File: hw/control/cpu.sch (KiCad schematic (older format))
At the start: 2 parts

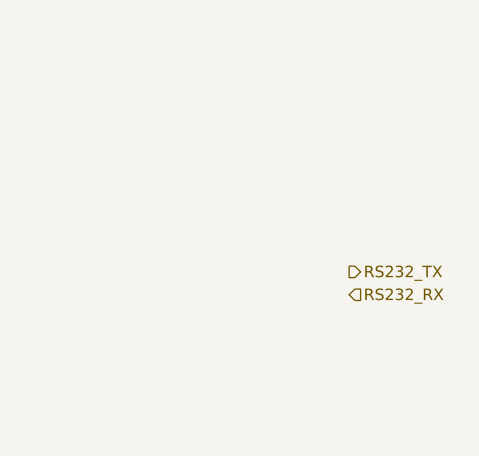
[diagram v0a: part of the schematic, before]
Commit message: [hw] Add LED bus driver
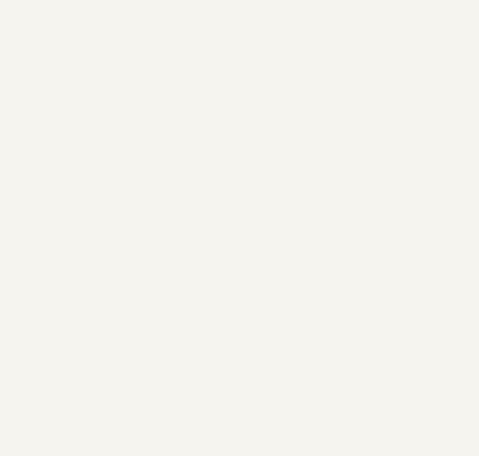
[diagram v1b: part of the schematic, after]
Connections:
- net labels removed: RS232_RX, RS232_TX
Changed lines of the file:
@@
 Wire Wire Line
 	5000 3450 6850 3450
-Text HLabel 9450 5000 2    50   Output ~ 0
-RS232_TX
-Text HLabel 9450 5100 2    50   Input ~ 0
-RS232_RX
 $EndSCHEMATC

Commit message: [hw] Add secondary SD card connection
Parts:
- added C?: 100n, symbol Device:C
- added J?: Conn_01x03_Male, symbol Connector:Conn_01x03_Male
- added J?: Micro_SD_Card, symbol Connector:Micro_SD_Card
- added R? (x6): 33R, symbol Device:R
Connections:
- wire segments 34 -> 80
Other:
- moved on the sheet: J?

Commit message: [hw] Add annotations, minor fixes
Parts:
- removed J?: Raspberry_Pi_2_3, symbol Connector:Raspberry_Pi_2_3
- added C301, C302, C303, C304: 100n, symbol Device:C
- added J303: Raspberry_Pi_0_2_3, symbol my:Raspberry_Pi_0_2_3
- gave numbers to parts that had none: 10
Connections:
- wire segments 80 -> 108
- no-connect marks 0 -> 3

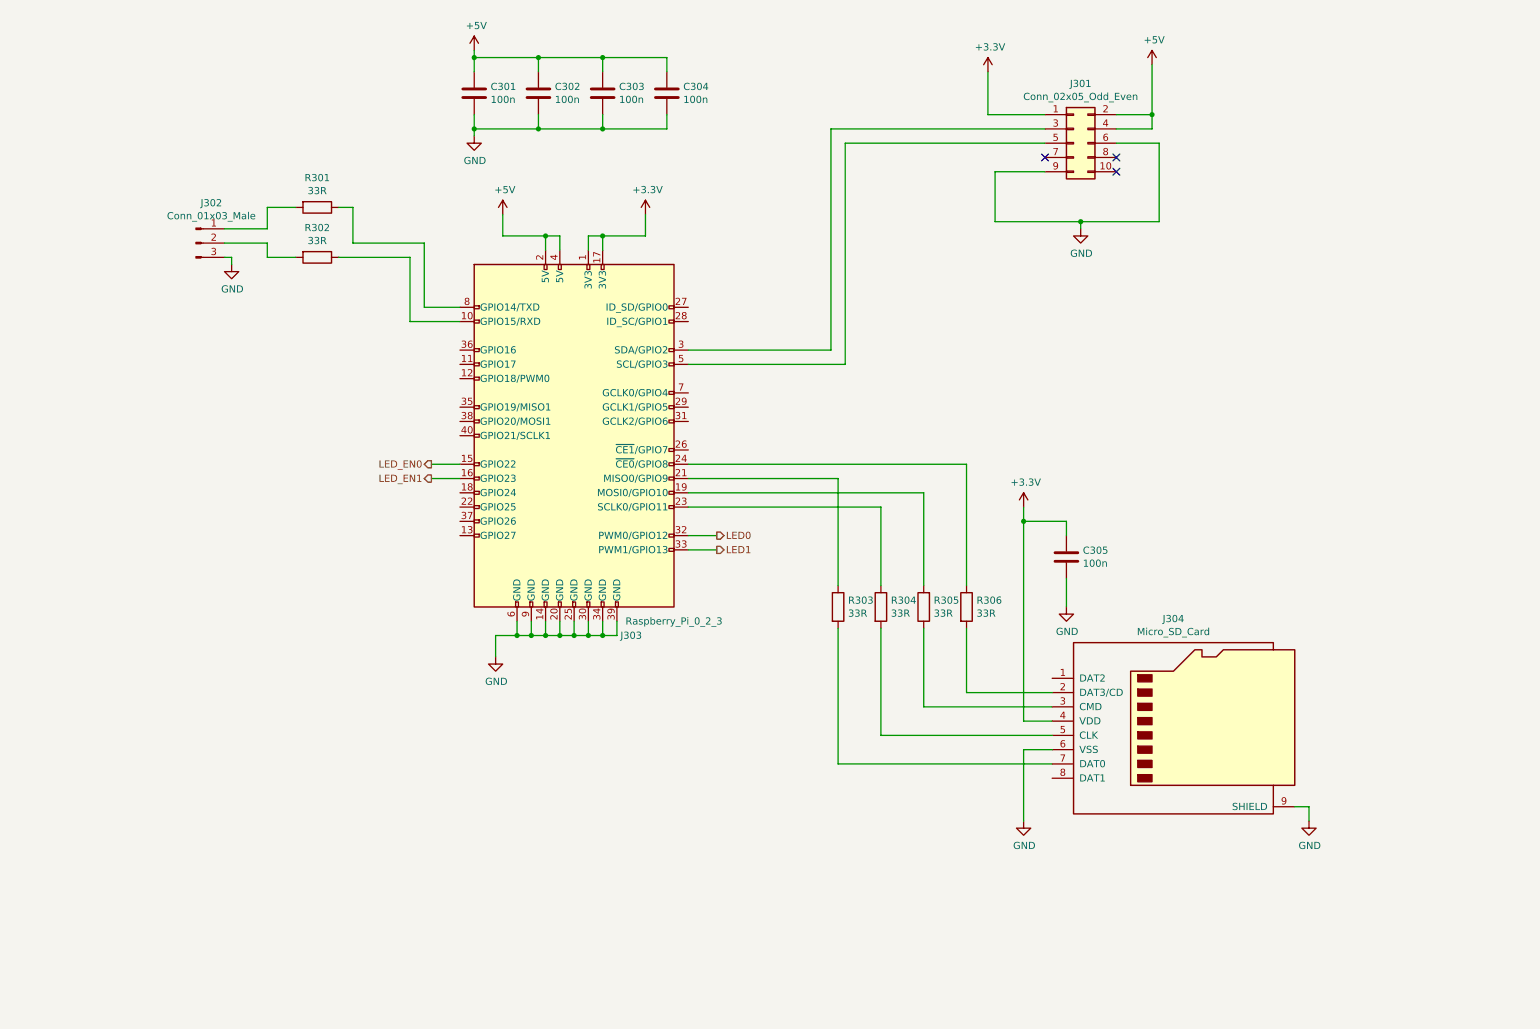
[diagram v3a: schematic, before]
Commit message: [hw] Add LED driver output sheets
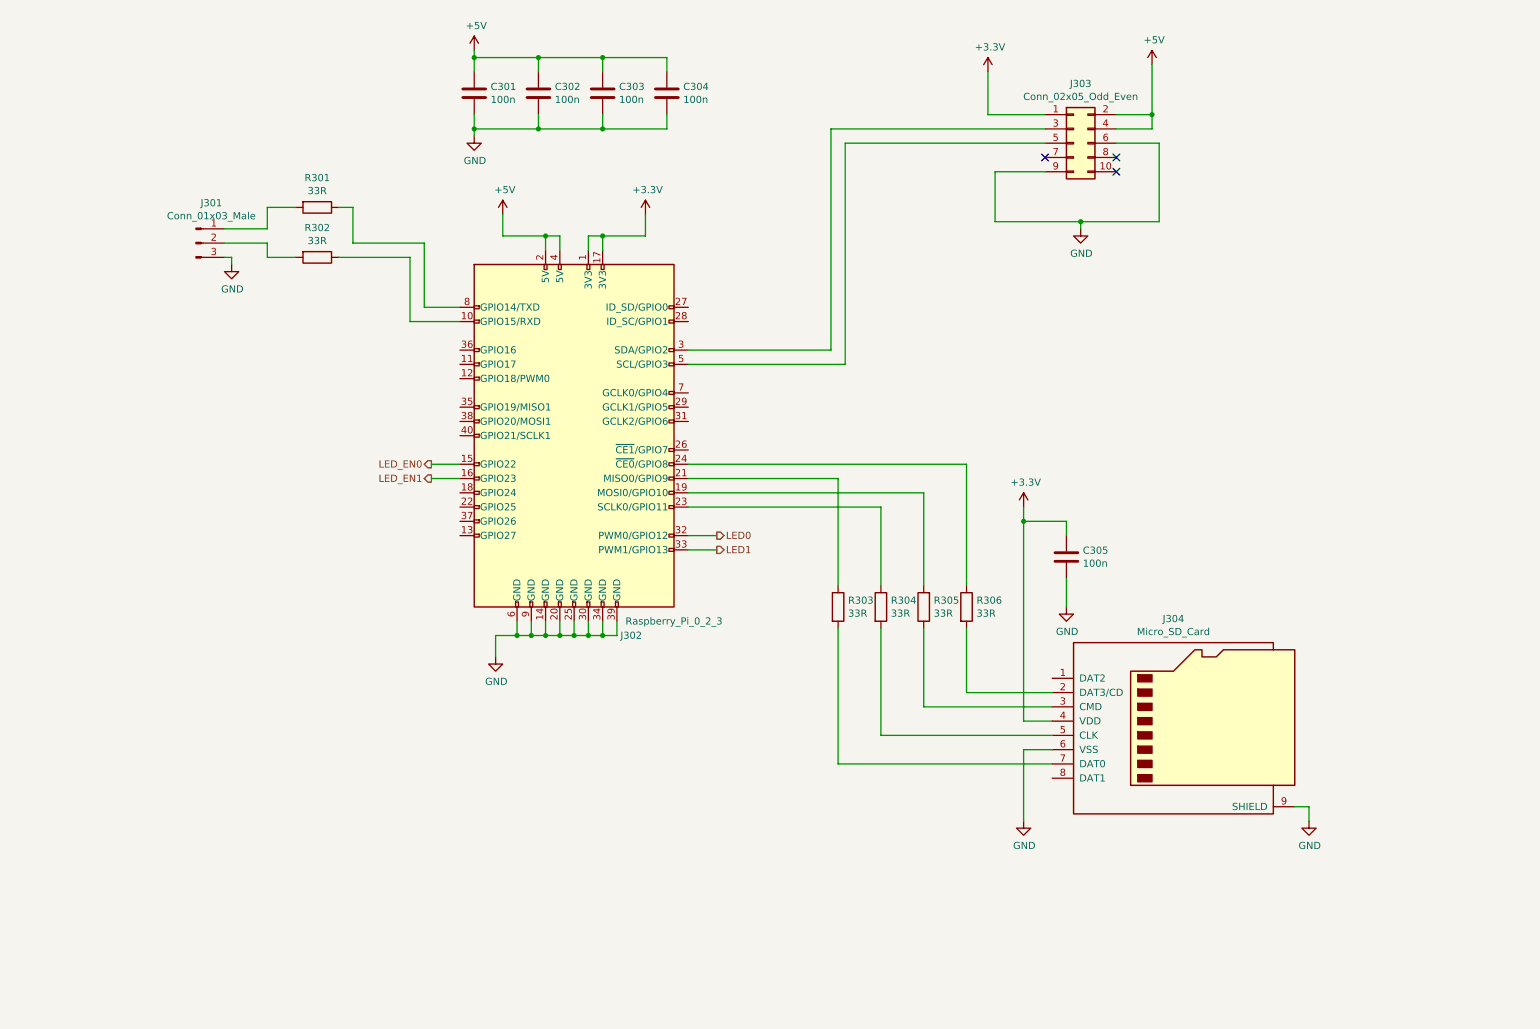
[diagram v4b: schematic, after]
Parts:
- renumbered J302 to J301, J303 to J302, J301 to J303
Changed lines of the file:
@@
 $Descr A4 11693 8268
 encoding utf-8
-Sheet 3 7
+Sheet 3 9
 Title "WS2812 Controller"
-Date "2021-09-16"
+Date "2021-09-21"
 Rev "1"
 Comp "Stefan Misik"
@@
 P 3950 5100
 AR Path="/614A2C71" Ref="#PWR?"  Part="1"
-AR Path="/6148E1AC/614A2C71" Ref="#PWR0311"  Part="1"
-F 0 "#PWR0311" H 3950 4850 50  0001 C CNN
+AR Path="/6148E1AC/614A2C71" Ref="#PWR0304"  Part="1"
+F 0 "#PWR0304" H 3950 4850 50  0001 C CNN
 F 1 "GND" H 3955 4927 50  0000 C CNN
 F 2 "" H 3950 5100 50  0001 C CNN
@@
 P 8000 1500
 AR Path="/614A2C9B" Ref="J?"  Part="1"
-AR Path="/6148E1AC/614A2C9B" Ref="J301"  Part="1"
-F 0 "J301" H 8050 1917 50  0000 C CNN
+AR Path="/6148E1AC/614A2C9B" Ref="J303"  Part="1"
+F 0 "J303" H 8050 1917 50  0000 C CNN
 F 1 "Conn_02x05_Odd_Even" H 8050 1826 50  0000 C CNN
 F 2 "" H 8000 1500 50  0001 C CNN
@@
 P 8550 950
 AR Path="/614A2CA1" Ref="#PWR?"  Part="1"
-AR Path="/6148E1AC/614A2CA1" Ref="#PWR0302"  Part="1"
-F 0 "#PWR0302" H 8550 800 50  0001 C CNN
+AR Path="/6148E1AC/614A2CA1" Ref="#PWR0312"  Part="1"
+F 0 "#PWR0312" H 8550 800 50  0001 C CNN
 F 1 "+5V" H 8565 1123 50  0000 C CNN
 F 2 "" H 8550 950 50  0001 C CNN
@@
 P 7400 1000
 AR Path="/614A2CA7" Ref="#PWR?"  Part="1"
-AR Path="/6148E1AC/614A2CA7" Ref="#PWR0303"  Part="1"
-F 0 "#PWR0303" H 7400 850 50  0001 C CNN
+AR Path="/6148E1AC/614A2CA7" Ref="#PWR0307"  Part="1"
+F 0 "#PWR0307" H 7400 850 50  0001 C CNN
 F 1 "+3.3V" H 7415 1173 50  0000 C CNN
 F 2 "" H 7400 1000 50  0001 C CNN
@@
 P 8050 2100
 AR Path="/614A2CB4" Ref="#PWR?"  Part="1"
-AR Path="/6148E1AC/614A2CB4" Ref="#PWR0307"  Part="1"
-F 0 "#PWR0307" H 8050 1850 50  0001 C CNN
+AR Path="/6148E1AC/614A2CB4" Ref="#PWR0311"  Part="1"
+F 0 "#PWR0311" H 8050 1850 50  0001 C CNN
 F 1 "GND" H 8055 1927 50  0000 C CNN
 F 2 "" H 8050 2100 50  0001 C CNN
@@
 LED_EN1
 $Comp
-L Connector:Conn_01x03_Male J302
+L Connector:Conn_01x03_Male J301
 U 1 1 614671E5
 P 1850 2200
-F 0 "J302" H 1958 2481 50  0000 C CNN
+F 0 "J301" H 1958 2481 50  0000 C CNN
 F 1 "Conn_01x03_Male" H 1958 2390 50  0000 C CNN
 F 2 "" H 1850 2200 50  0001 C CNN
@@
 $EndComp
 $Comp
-L power:GND #PWR0308
+L power:GND #PWR0301
 U 1 1 6146B045
 P 2100 2350
-F 0 "#PWR0308" H 2100 2100 50  0001 C CNN
+F 0 "#PWR0301" H 2100 2100 50  0001 C CNN
 F 1 "GND" H 2105 2177 50  0000 C CNN
 F 2 "" H 2100 2350 50  0001 C CNN
@@
 	6950 3950 6950 4600
 $Comp
-L power:+3.3V #PWR0309
+L power:+3.3V #PWR0308
 U 1 1 614C61E8
 P 7650 4050
-F 0 "#PWR0309" H 7650 3900 50  0001 C CNN
+F 0 "#PWR0308" H 7650 3900 50  0001 C CNN
 F 1 "+3.3V" H 7665 4223 50  0000 C CNN
 F 2 "" H 7650 4050 50  0001 C CNN
@@
 Connection ~ 7650 4150
 $Comp
-L power:GND #PWR0312
+L power:GND #PWR0309
 U 1 1 614D028A
 P 7650 6250
-F 0 "#PWR0312" H 7650 6000 50  0001 C CNN
+F 0 "#PWR0309" H 7650 6000 50  0001 C CNN
 F 1 "GND" H 7655 6077 50  0000 C CNN
 F 2 "" H 7650 6250 50  0001 C CNN
@@
 $EndComp
 $Comp
-L power:+5V #PWR0301
+L power:+5V #PWR0302
 U 1 1 61473572
 P 3800 850
-F 0 "#PWR0301" H 3800 700 50  0001 C CNN
+F 0 "#PWR0302" H 3800 700 50  0001 C CNN
 F 1 "+5V" H 3815 1023 50  0000 C CNN
 F 2 "" H 3800 850 50  0001 C CNN
@@
 $EndComp
 $Comp
-L power:GND #PWR0304
+L power:GND #PWR0303
 U 1 1 61474A2C
 P 3800 1450
-F 0 "#PWR0304" H 3800 1200 50  0001 C CNN
+F 0 "#PWR0303" H 3800 1200 50  0001 C CNN
 F 1 "GND" H 3805 1277 50  0000 C CNN
 F 2 "" H 3800 1450 50  0001 C CNN
@@
 Connection ~ 4700 900
 $Comp
-L my:Raspberry_Pi_0_2_3 J303
+L my:Raspberry_Pi_0_2_3 J302
 U 1 1 614A89DF
 P 4500 3550
-F 0 "J303" H 4900 2150 50  0000 C CNN
+F 0 "J302" H 4900 2150 50  0000 C CNN
 F 1 "Raspberry_Pi_0_2_3" H 5200 2250 50  0000 C CNN
 F 2 "" H 4500 3550 50  0001 C CNN

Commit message: [hw] Add some more peripherals
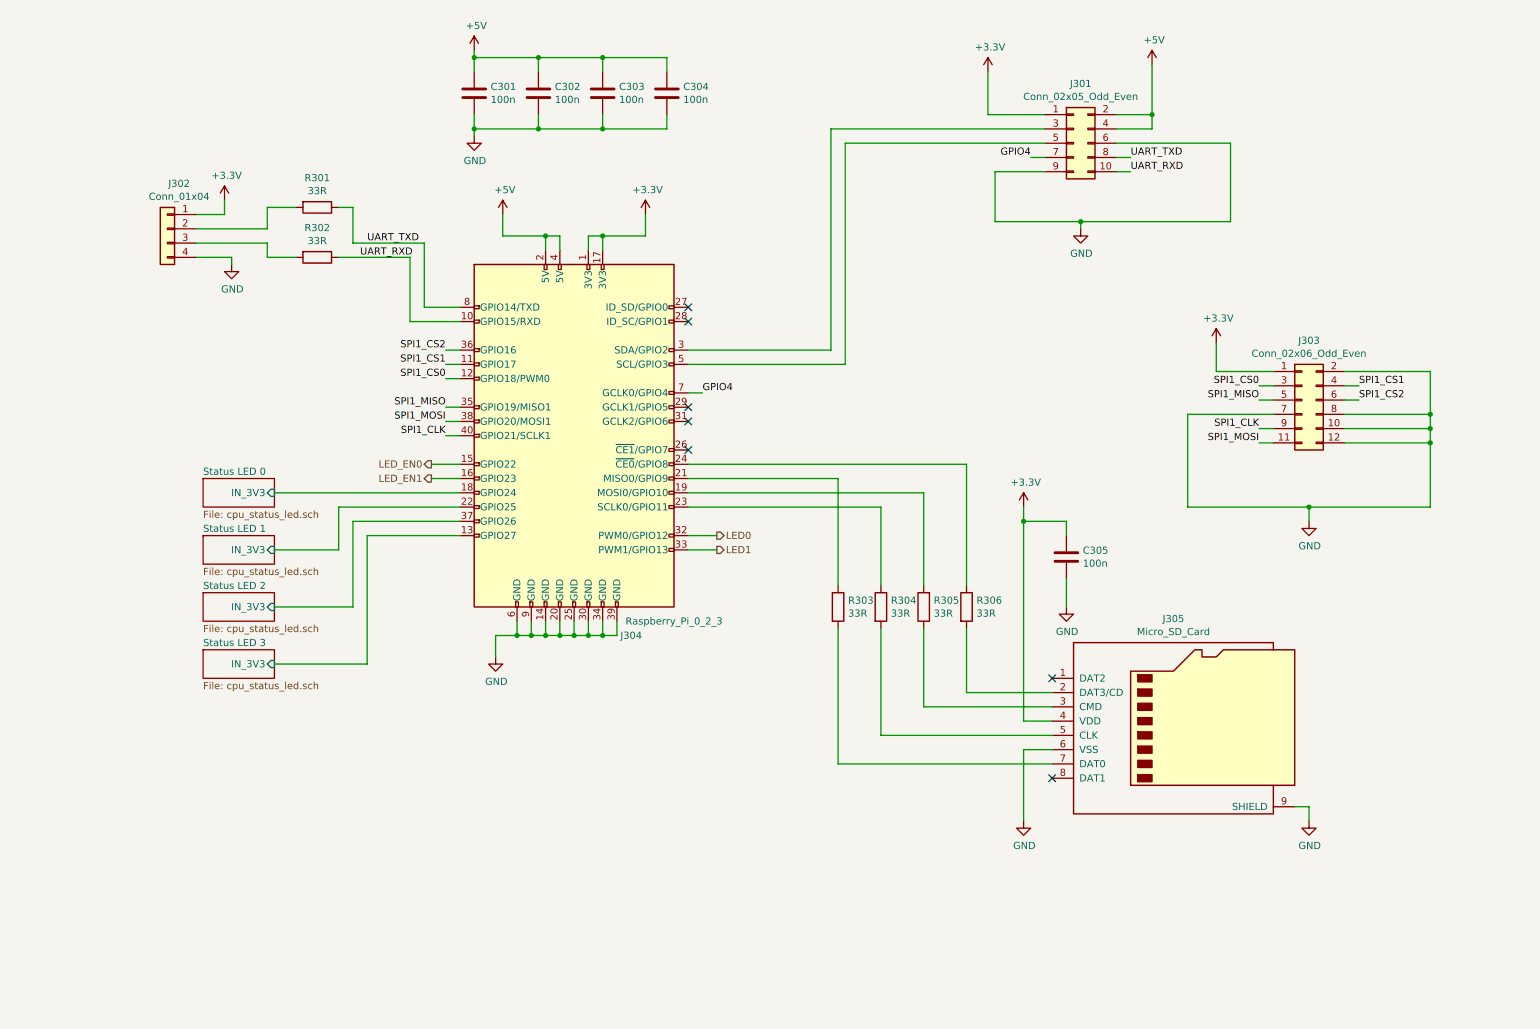
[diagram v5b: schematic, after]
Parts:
- removed J301: Conn_01x03_Male, symbol Connector:Conn_01x03_Male
- added J302: Conn_01x04, symbol Connector_Generic:Conn_01x04
- added J303: Conn_02x06_Odd_Even, symbol Connector_Generic:Conn_02x06_Odd_Even
- renumbered J303 to J301, J302 to J304, J304 to J305
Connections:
- net +3V3: now also J302.1 (Pin_1), J303.1 (Pin_1)
- net GND: now also J302.4 (Pin_4), J303.10 (Pin_10), J303.12 (Pin_12), J303.2 (Pin_2), J303.7 (Pin_7), J303.8 (Pin_8)
- net at R301.2: now also J302.2 (Pin_2)
- net at R302.2: now also J302.3 (Pin_3)
- net UART_RXD: now reaches J304.10 (GPIO15/RXD), R302.1
- net UART_RXD: now also J301.10 (Pin_10)
- net UART_TXD: now reaches J304.8 (GPIO14/TXD), R301.1
- net UART_TXD: now also J301.8 (Pin_8)
- net GPIO4: now reaches J301.7 (Pin_7)
- net GPIO4: now also J304.7 (GCLK0/GPIO4)
- net SPI1_CS1: now reaches J304.11 (GPIO17)
- net SPI1_CS1: now also J303.4 (Pin_4)
- net SPI1_CS0: now reaches J304.12 (GPIO18/PWM0)
- net SPI1_CS0: now also J303.3 (Pin_3)
- net Status LED 3/IN_3V3: now reaches J304.13 (GPIO27)
- net Status LED 0/IN_3V3: now reaches J304.18 (GPIO24)
- net Status LED 1/IN_3V3: now reaches J304.22 (GPIO25)
- net SPI1_MISO: now reaches J304.35 (GPIO19/MISO1)
- net SPI1_MISO: now also J303.5 (Pin_5)
- net SPI1_CS2: now reaches J304.36 (GPIO16)
- net SPI1_CS2: now also J303.6 (Pin_6)
- net Status LED 2/IN_3V3: now reaches J304.37 (GPIO26)
- net SPI1_MOSI: now reaches J304.38 (GPIO20/MOSI1)
- net SPI1_MOSI: now also J303.11 (Pin_11)
- net SPI1_CLK: now reaches J304.40 (GPIO21/SCLK1)
- net SPI1_CLK: now also J303.9 (Pin_9)
- no-connect marks 3 -> 7

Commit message: [hw] Add alternative LED data line from SPI
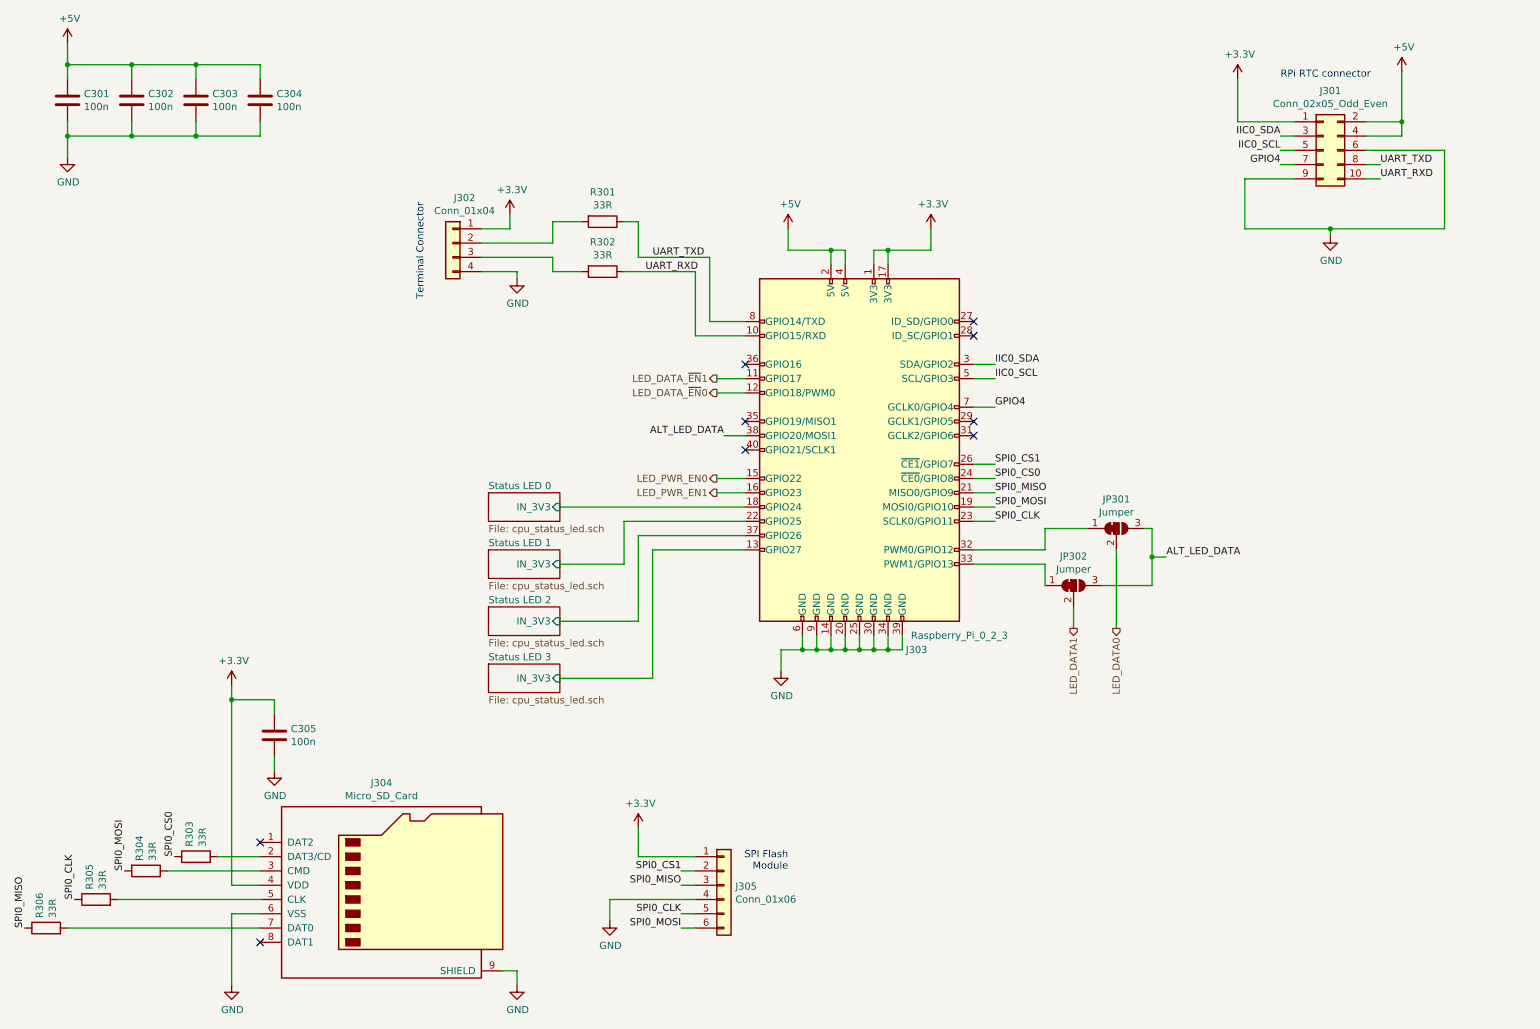
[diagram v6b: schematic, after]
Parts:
- removed J303: Conn_02x06_Odd_Even, symbol Connector_Generic:Conn_02x06_Odd_Even
- added J305: Conn_01x06, symbol Connector_Generic:Conn_01x06
- added JP301, JP302: Jumper, symbol Jumper:SolderJumper_3_Bridged12
- renumbered J304 to J303, J305 to J304, R306 to R303, R305 to R304, R304 to R305, R303 to R306
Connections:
- net +3V3: now also J305.1 (Pin_1)
- net GND: now also J305.4 (Pin_4)
- net SPI0_MOSI: now reaches J303.19 (MOSI0/GPIO10), R304.2
- net SPI0_MOSI: now also J305.6 (Pin_6)
- net SPI0_CLK: now reaches J303.23 (SCLK0/GPIO11), R305.1
- net SPI0_CLK: now also J305.5 (Pin_5)
- net SPI0_MISO: now reaches J303.21 (MISO0/GPIO9), R306.1
- net SPI0_MISO: now also J305.3 (Pin_3)
- net SPI0_CS0: now reaches J303.24 (~CE0~/GPIO8), R303.1
- net IIC0_SDA: now reaches J301.3 (Pin_3), J303.3 (SDA/GPIO2)
- net IIC0_SCL: now reaches J301.5 (Pin_5), J303.5 (SCL/GPIO3)
- net SPI0_CS1: now reaches J303.26 (~CE1~/GPIO7)
- net SPI0_CS1: now also J305.2 (Pin_2)
- net LED0: no longer names the net of J303.32 (PWM0/GPIO12)
- net LED0: now also JP301.1 (A)
- net LED1: no longer names the net of J303.33 (PWM1/GPIO13)
- net LED1: now also JP302.1 (A)
- net LED_EN0 renamed LED_PWR_EN0
- net LED_EN1 renamed LED_PWR_EN1
- net SPI1_CLK: no longer names the net of J303.40 (GPIO21/SCLK1)
- net SPI1_CS0 renamed LED_DATA_~EN~0
- net SPI1_CS1 renamed LED_DATA_~EN~1
- net SPI1_CS2: no longer names the net of J303.36 (GPIO16)
- net SPI1_MISO: no longer names the net of J303.35 (GPIO19/MISO1)
- net SPI1_MOSI renamed ALT_LED_DATA
- net ALT_LED_DATA: now also JP301.3 (B), JP302.3 (B)
- new net LED_DATA0: JP301.2 (C)
- new net LED_DATA1: JP302.2 (C)
- no-connect marks 7 -> 9
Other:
- note added: "RPi RTC connector"
- note added: "SPI Flash\nModule"
- note added: "Terminal Connector"
- moved on the sheet: C301, C302, C303, C304, C305, J301, J302, J303, J304, R301, R302, R303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
